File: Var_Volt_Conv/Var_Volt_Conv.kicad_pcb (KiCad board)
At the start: 6 copper layers, 98 parts, among them J101 Jack-DC, J102 Screw_Terminal_01x02, J103 Screw_Terminal_01x02, J201 Conn_01x05, Q101 AO3416, Q102 IRFML8244TRPBF, Q103 IRFML8244TRPBF, Q104 AO3407, Q105 AO3407, Q106 AO3407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

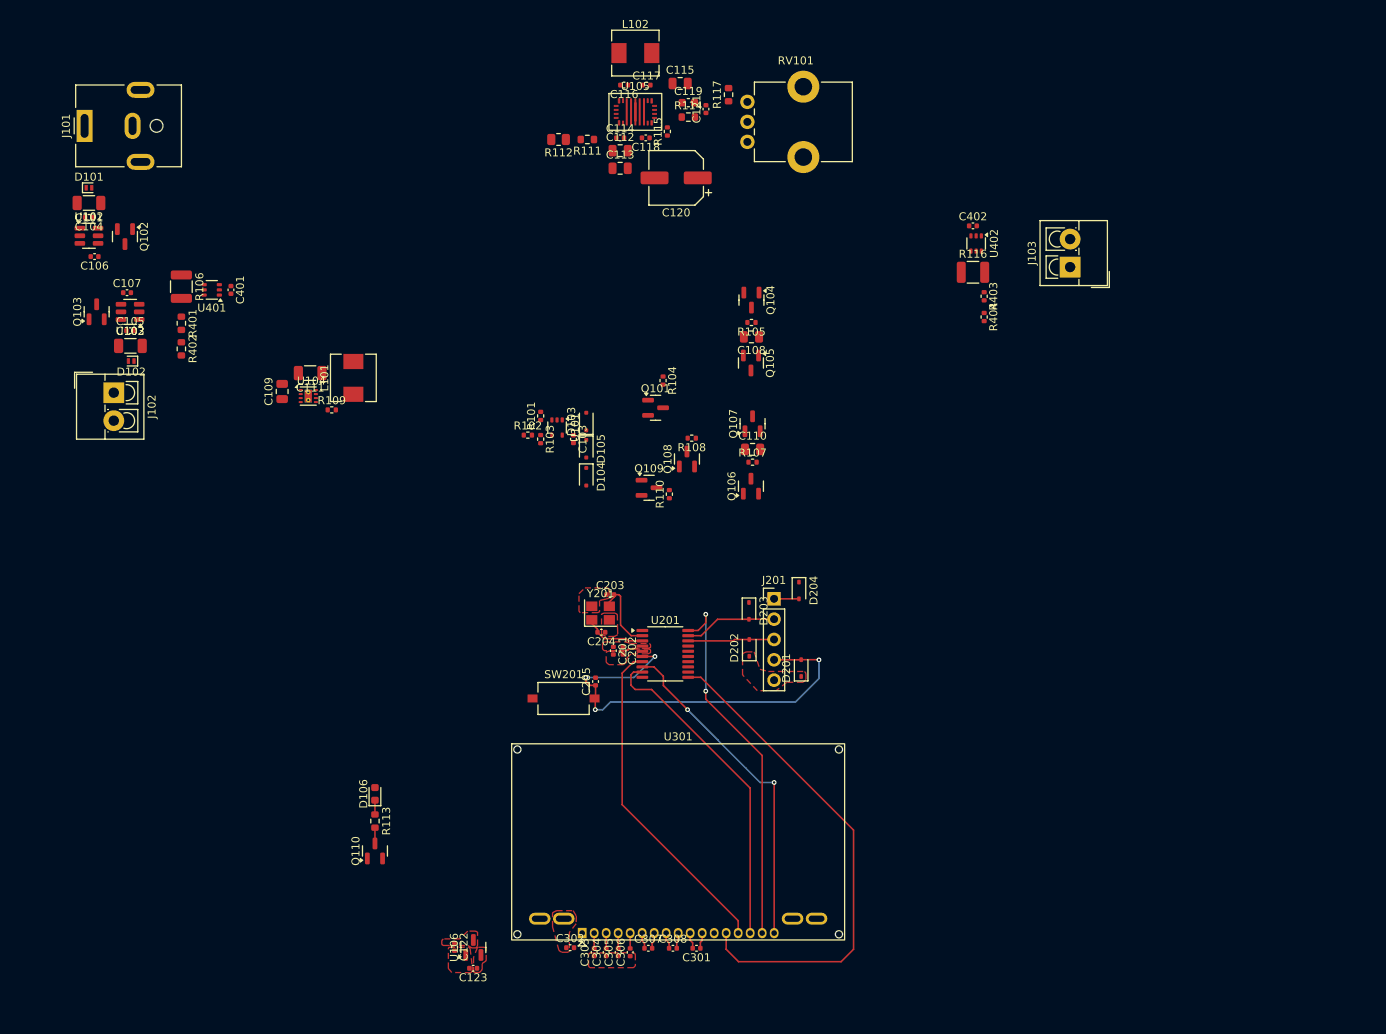
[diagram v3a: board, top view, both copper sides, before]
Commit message: Routed Input system power circuitry, and named the LM74700 gate connection nets
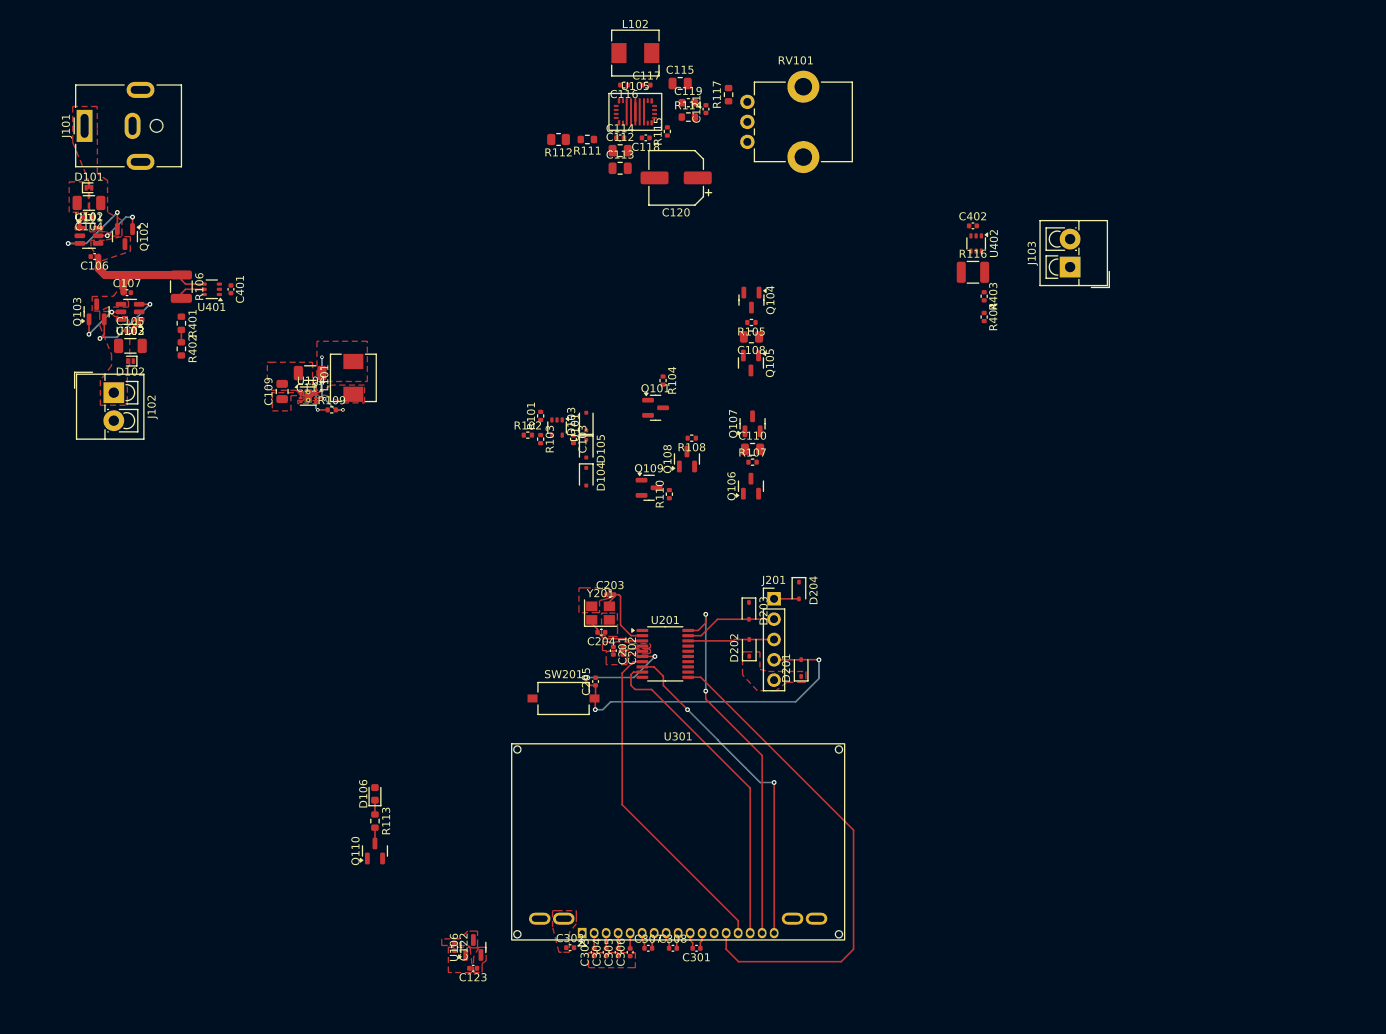
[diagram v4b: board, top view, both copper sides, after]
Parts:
- moved D102 0.10 mm to (32.6, 63.1)
- moved C401 0.08 mm to (45.2, 54.1)
- moved U401 0.08 mm to (42.8, 54.1)
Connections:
- net Net-(Q102-G) renamed /[1] Power/GATE_J
- net Net-(Q103-G) renamed /[1] Power/GATE_T
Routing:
- net SYSTEM_POWER_A: track 0.00 -> 18.5 mm
- net /[1] Power/SCREW_TERMINAL_POWER: track 0.00 -> 12.0 mm, vias 0 -> 2
- net /[1] Power/JACK_POWER: track 0.00 -> 11.3 mm, vias 0 -> 2
- net /[1] Power/BUCK_VOS: track 0.00 -> 10.2 mm, vias 0 -> 3
- net /[1] Power/GATE_T: track 0.00 -> 7.04 mm, vias 0 -> 2
- net /[1] Power/GATE_J: track 0.00 -> 6.78 mm, vias 0 -> 2
- net /[1] Power/PG: track 0.00 -> 5.31 mm, vias 0 -> 2
- net SYSTEM_POWER_B: track 0.00 -> 4.18 mm
- net /[1] Power/VCAP_J: track 0.00 -> 1.82 mm
- net /[1] Power/VCAP_T: track 0.00 -> 1.67 mm
- net S-INPUT_VOLTAGE: track 0.00 -> 1.55 mm
- added copper zone on F.Cu, net /[1] Power/BUCK_SW
- added copper zone on F.Cu, net /[1] Power/BUCK_VOS
- added copper zone on F.Cu, net /[1] Power/JACK_POWER
- added copper zone on F.Cu, net /[1] Power/SCREW_TERMINAL_POWER
- added copper zone on F.Cu, net SYSTEM_POWER_A
- added copper zone on F.Cu, net SYSTEM_POWER_B

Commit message: Finished tracing priority 3.3V power multiplexer, changed terminal block footprints to 5.00mm pitch
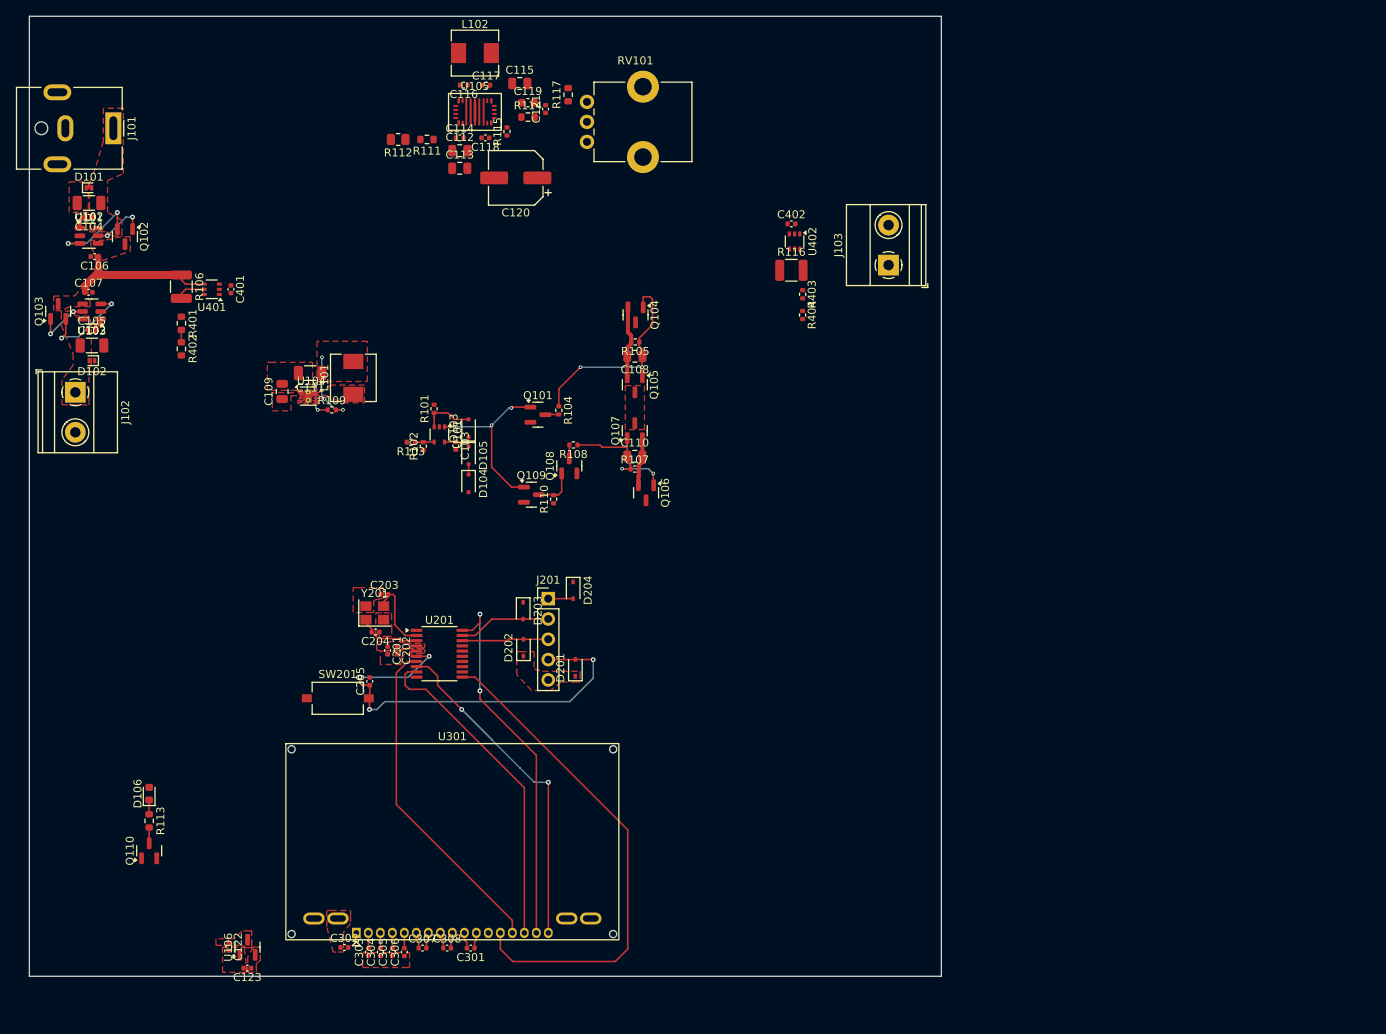
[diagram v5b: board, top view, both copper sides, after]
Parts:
- J102, J103: footprint TerminalBlock_4Ucon:TerminalBlock_4Ucon_1x02_P3.50mm_Vertical -> TerminalBlock_Phoenix:TerminalBlock_Phoenix_MKDS-1,5-2_1x02_P5.00mm_Horizontal
- moved C122 28.2 mm to (44.9, 136.3)
- moved C202 28.2 mm to (66.0, 99.3)
- moved C205 28.2 mm to (62.5, 103.1)
- moved C307 28.2 mm to (69.1, 136.5)
- moved D203 28.2 mm to (81.7, 94.3)
- moved D204 28.2 mm to (88.0, 91.8)
- moved J201 28.2 mm to (84.9, 92.8)
- moved SW201 28.2 mm to (58.5, 105.2)
- moved Y201 28.2 mm to (63.2, 94.6)
- moved C204 28.2 mm to (63.3, 97.0)
- moved D106 28.2 mm to (35.0, 117.2)
- moved Q110 28.2 mm to (35.0, 124.3)
- moved R113 28.2 mm to (35.0, 120.6)
- moved U106 28.2 mm to (47.3, 136.4)
- moved C123 28.2 mm to (47.2, 139.0)
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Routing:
- net /[1] Power/BUCK_PPM_GATE: track 0.00 -> 26.9 mm, vias 0 -> 2
- net /[1] Power/COMP_OUT: track 0.00 -> 22.1 mm, vias 0 -> 3
- net /[1] Power/ST_PPM_GATE: track 0.00 -> 17.1 mm, vias 0 -> 2
- net /[1] Power/BUCK_PPM_SOURCE: track 0.00 -> 9.11 mm
- net /[1] Power/BUCK_VOS: track 10.2 -> 16.6 mm
- net /[1] Power/ST_PPM_SOURCE: track 0.00 -> 6.09 mm
- net /[1] Power/ST_PPM_INV1: track 0.00 -> 5.33 mm
- net /[1] Power/COMP_POWER: track 0.00 -> 4.21 mm
- net SYSTEM_POWER_A: track 18.5 -> 21.3 mm
- net /[1] Power/ST_PPM_IN: track 0.00 -> 2.41 mm
- net /[1] Power/BUCK_PPM_INV: track 0.00 -> 1.70 mm
- net /[1] Power/ST_PPM_INV2: track 0.00 -> 1.68 mm
- net /[1] Power/ST_3V3_Diode: track 0.00 -> 1.30 mm
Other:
- board outline added: 114 x 120 mm

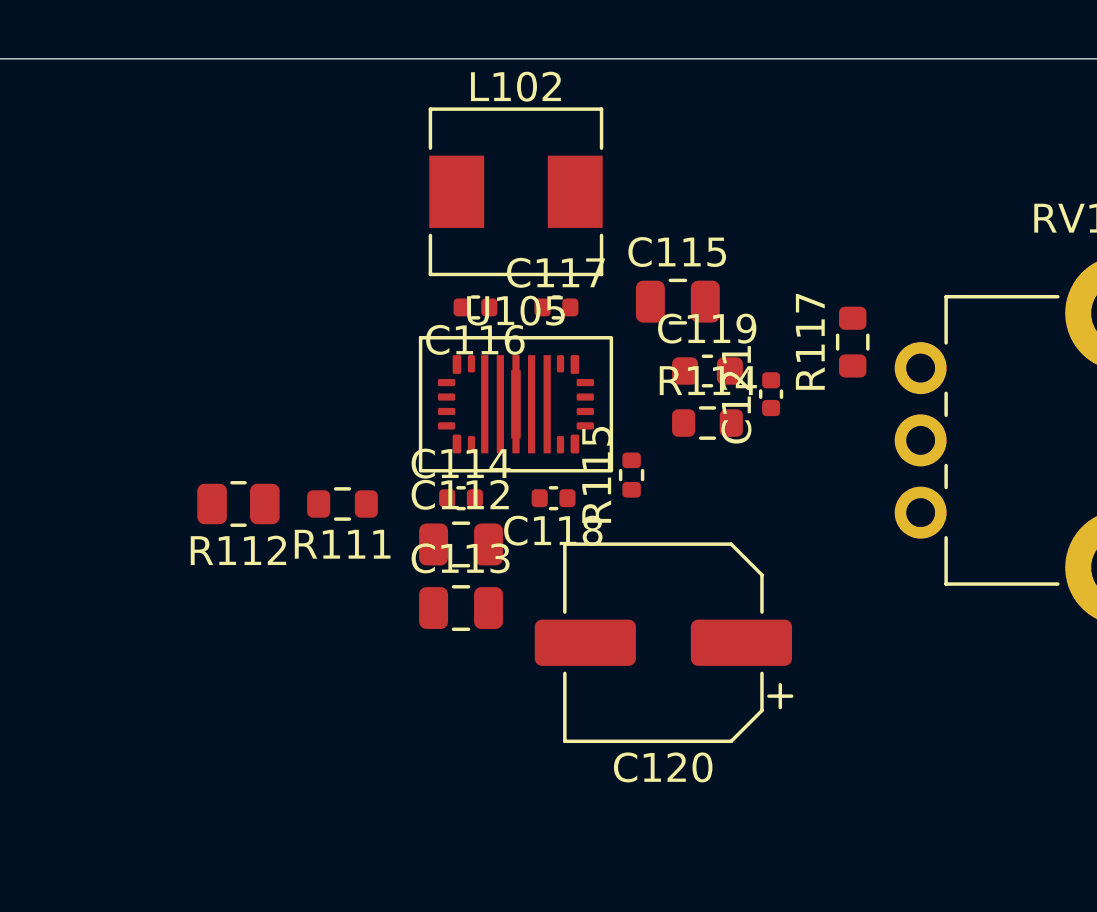
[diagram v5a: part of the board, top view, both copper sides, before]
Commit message: Finished traces buck-boost converter, add 3D model of the converter as well
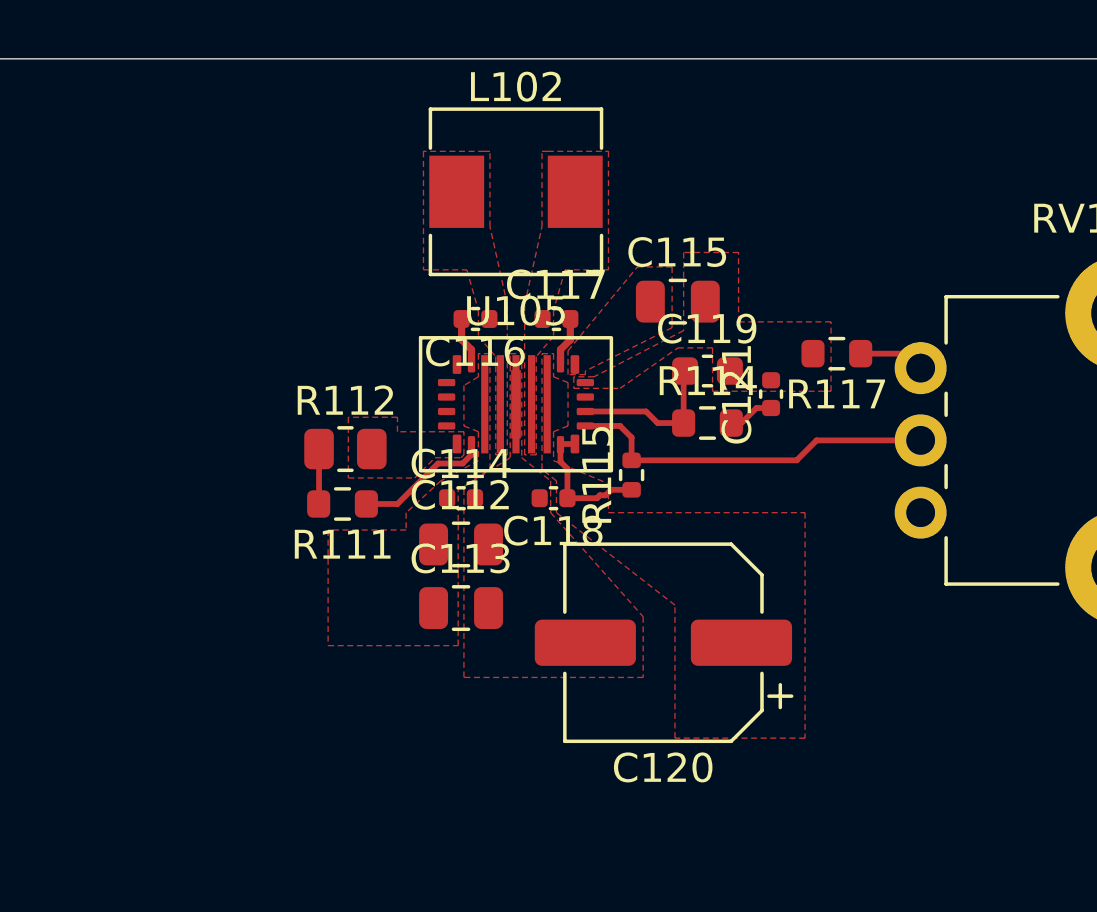
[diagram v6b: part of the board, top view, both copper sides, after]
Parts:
- moved R112 4.16 mm to (69.8, 33.5), turned to 0 degrees
- moved R117 0.68 mm to (86.8, 30.2), turned to 180 degrees
- moved C116 0.40 mm to (74.3, 29.0)
- moved C117 0.40 mm to (77.1, 29.0)
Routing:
- net /[1] Power/BB_FEEDBACK: track 0.00 -> 12.8 mm
- net /[1] Power/BB_COMP1: track 0.00 -> 5.39 mm
- net VARIABLE_OUTPUT_VOLTAGE_A: track 0.00 -> 4.80 mm
- net /[1] Power/BB_FSW1: track 0.00 -> 4.69 mm
- net /[1] Power/BB_POT_R: track 0.00 -> 2.28 mm
- net /[1] Power/BB_FSW2: track 0.00 -> 1.91 mm
- net /[1] Power/BB_BOOT2: track 0.00 -> 1.69 mm
- net /[1] Power/BB_BOOT1: track 0.00 -> 1.69 mm
- net /[1] Power/BB_COMP2: track 0.00 -> 1.59 mm
- added copper zone on F.Cu, net /[1] Power/BB_SW1
- added copper zone on F.Cu, net /[1] Power/BB_SW2
- added copper zone on F.Cu, net /[1] Power/VCC_BB
- added copper zone on F.Cu, net VARIABLE_OUTPUT_VOLTAGE_A

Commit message: Finish tracing all individual sub-circuits
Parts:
- moved R116 32.0 mm to (83.5, 48.0), turned to -90 degrees
- moved U402 28.7 mm to (87.0, 48.4), turned to 180 degrees
- moved C402 26.2 mm to (89.2, 48.0), turned to -90 degrees
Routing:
- net VARIABLE_OUTPUT_VOLTAGE_B: track 0.00 -> 3.31 mm
- net VARIABLE_OUTPUT_VOLTAGE_A: track 4.80 -> 8.10 mm
- net S-OUTPUT_VOLTAGE: track 0.00 -> 1.57 mm
